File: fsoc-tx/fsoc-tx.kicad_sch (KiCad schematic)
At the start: 0 parts

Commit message: TX ROOT: MCU clock and POWER USB
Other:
- added sheet TX_LASER (tx_laser.kicad_sch)
- added sheet TX_MCU_CLOCK (tx_mcu_clock.kicad_sch)
- added sheet TX_POWER_USB (tx_power_usb.kicad_sch)
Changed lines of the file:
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@@
 	(generator_version "10.0")
 	(paper "A4")
+	(sheet
+		(at 118.11 31.75)
+		(size 40.64 49.53)
+		(exclude_from_sim no)
+		(in_bom yes)
+		(on_board yes)
+		(dnp no)
+		(fields_autoplaced yes)
+		(stroke
+			(width 0.1524)
+			(type solid)
+		)
+		(fill
+			(color 0 0 0 0)
+		)
+		(property "Sheetname" "TX_MCU_CLOCK"
+			(at 118.11 31.0384 0)
+			(show_name no)
+			(do_not_autoplace no)
+			(effects
+				(font
+					(size 1.27 1.27)
+				)
+				(justify left bottom)
+			)
+		)
+		(property "Sheetfile" "tx_mcu_clock.kicad_sch"
+			(at 118.11 81.8646 0)
+			(show_name no)
+			(do_not_autoplace no)
+			(effects
+				(font
+					(size 1.27 1.27)
+				)
+				(justify left top)
+			)
+		)
+		(instances
+			(project "fsoc-tx"
+				(path "/d92cb11a-a3ee-43a3-bd30-881774176ced"
+					(page "3")
+				)
+			)
+		)
+	)
+	(sheet
+		(at 58.42 30.48)
+		(size 39.37 52.07)
+		(exclude_from_sim no)
+		(in_bom yes)
+		(on_board yes)
+		(dnp no)
+		(fields_autoplaced yes)
+		(stroke
+			(width 0.1524)
+			(type solid)
+		)
+		(fill
+			(color 0 0 0 0)
+		)
+		(property "Sheetname" "TX_POWER_USB"
+			(at 58.42 29.7684 0)
+			(show_name no)
+			(do_not_autoplace no)
+			(effects
+				(font
+					(size 1.27 1.27)
+				)
+				(justify left bottom)
+			)
+		)
+		(property "Sheetfile" "tx_power_usb.kicad_sch"
+			(at 58.42 83.1346 0)
+			(show_name no)
+			(do_not_autoplace no)
+			(effects
+				(font
+					(size 1.27 1.27)
+				)
+				(justify left top)
+			)
+		)
+		(instances
+			(project "fsoc-tx"
+				(path "/d92cb11a-a3ee-43a3-bd30-881774176ced"
+					(page "2")
+				)
+			)
+		)
+	)
+	(sheet
+		(at 187.96 36.83)
+		(size 36.83 50.8)
+		(exclude_from_sim no)
+		(in_bom yes)
+		(on_board yes)
+		(dnp no)
+		(fields_autoplaced yes)
+		(stroke
+			(width 0.1524)
+			(type solid)
+		)
+		(fill
+			(color 0 0 0 0)
+		)
+		(property "Sheetname" "TX_LASER"
+			(at 187.96 36.1184 0)
+			(show_name no)
+			(do_not_autoplace no)
+			(effects
+				(font
+					(size 1.27 1.27)
+				)
+				(justify left bottom)
+			)
+		)
+		(property "Sheetfile" "tx_laser.kicad_sch"
+			(at 187.96 88.2146 0)
+			(show_name no)
+			(do_not_autoplace no)
+			(effects
+				(font
+					(size 1.27 1.27)
+				)
+				(justify left top)
+			)
+		)
+		(instances
+			(project "fsoc-tx"
+				(path "/d92cb11a-a3ee-43a3-bd30-881774176ced"
+					(page "4")
+				)
+			)
+		)
+	)
 	(sheet_instances
 		(path "/"

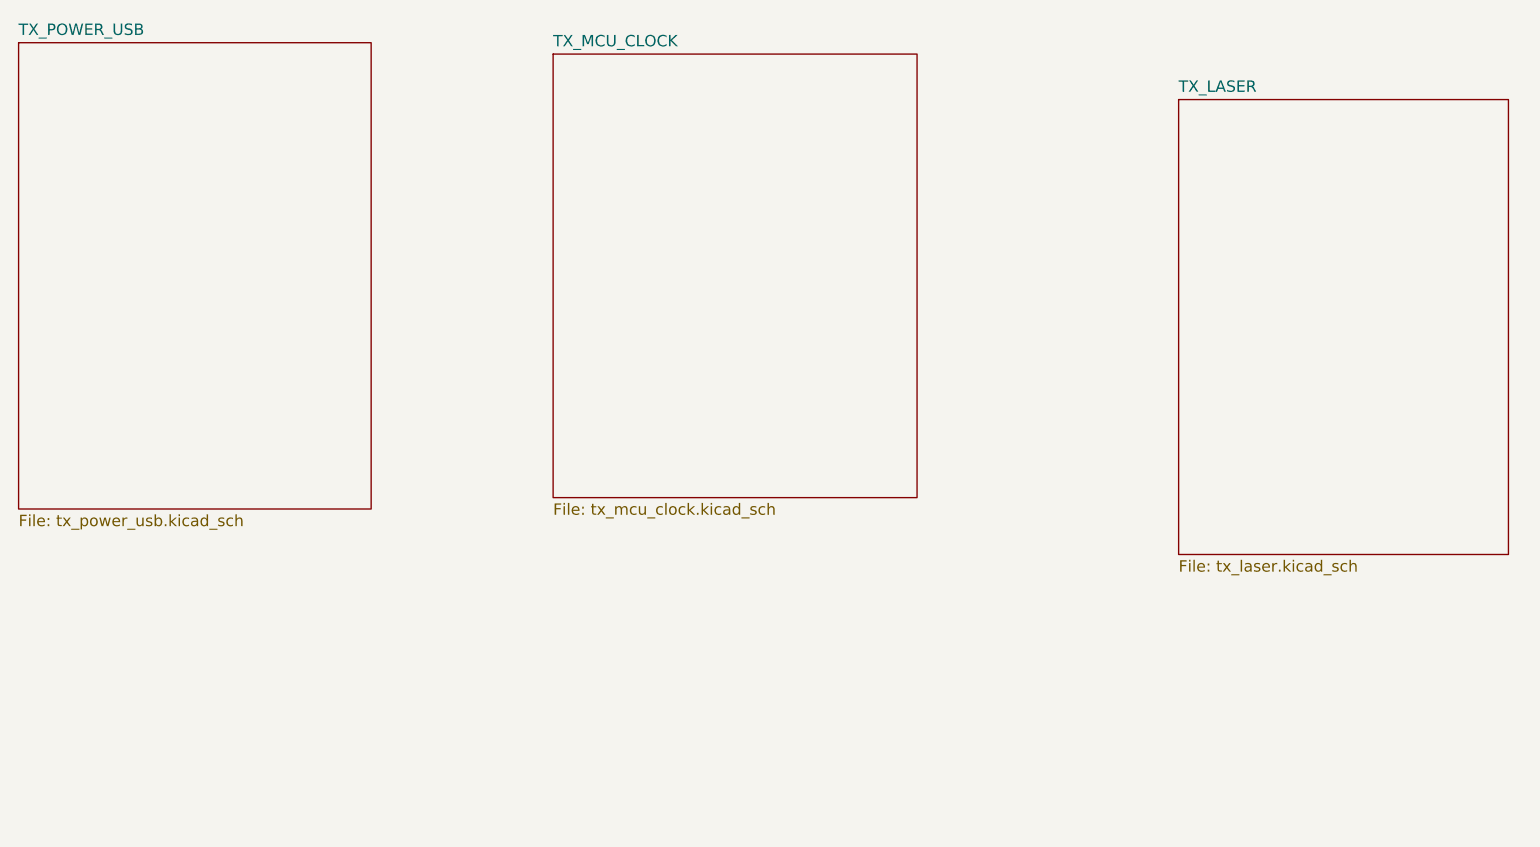
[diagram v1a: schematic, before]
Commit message: TX ROOT: laser + host IO
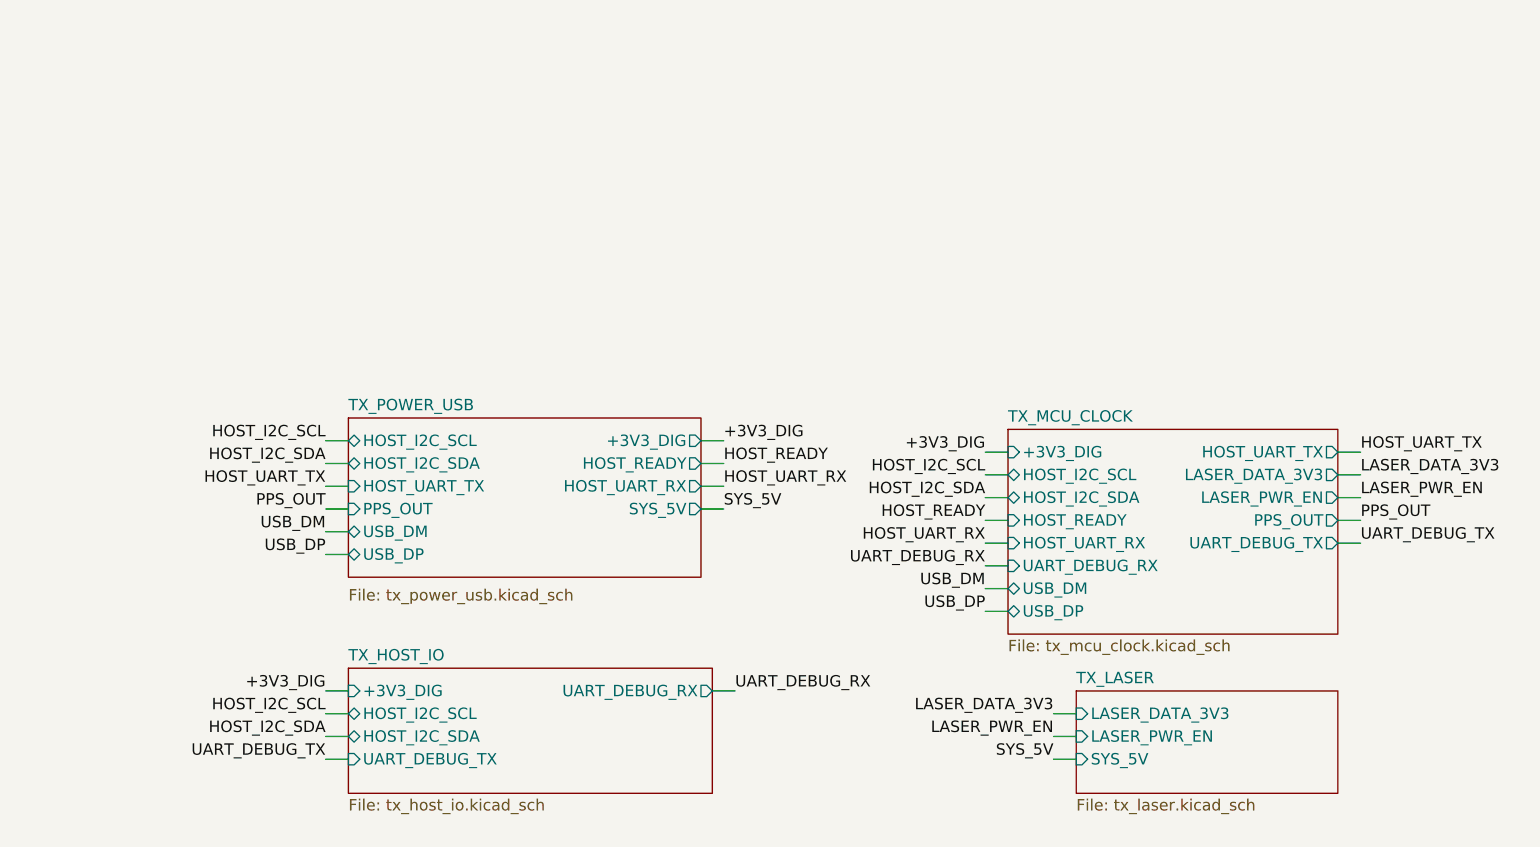
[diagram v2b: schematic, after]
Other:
- added sheet TX_HOST_IO (tx_host_io.kicad_sch)
- sheet TX_LASER ports: added LASER_DATA_3V3, LASER_PWR_EN, SYS_5V; removed none
- sheet TX_MCU_CLOCK ports: added +3V3_DIG, HOST_I2C_SCL, HOST_I2C_SDA, HOST_READY, HOST_UART_RX, HOST_UART_TX, LASER_DATA_3V3, LASER_PWR_EN, PPS_OUT, UART_DEBUG_RX, UART_DEBUG_TX, USB_DM, USB_DP; removed none
- sheet TX_POWER_USB ports: added +3V3_DIG, HOST_I2C_SCL, HOST_I2C_SDA, HOST_READY, HOST_UART_RX, HOST_UART_TX, PPS_OUT, SYS_5V, USB_DM, USB_DP; removed none

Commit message: TX PCB: DONE
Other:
- sheet TX_MCU_CLOCK ports: added USB_DN; removed USB_DM
- sheet TX_POWER_USB ports: added USB_DN; removed USB_DM
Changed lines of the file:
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@@
 		)
 	)
-	(label "USB_DM"
+	(label "USB_DN"
 		(at 92.71 85.09 180)
 		(effects
@@
 		)
 	)
-	(label "USB_DM"
+	(label "USB_DN"
 		(at 166.37 91.44 180)
 		(effects
@@
 	(sheet
 		(at 168.91 73.66)
-		(size 36.83 22.86)
+		(size 36.83 21.59)
 		(exclude_from_sim no)
 		(in_bom yes)
@@
 		)
 		(property "Sheetfile" "tx_mcu_clock.kicad_sch"
-			(at 168.91 97.1046 0)
+			(at 168.91 95.8346 0)
 			(show_name no)
 			(do_not_autoplace no)
@@
 			)
 		)
-		(pin "USB_DM" bidirectional
-			(at 168.91 91.44 180)
-			(effects
-				(font
-					(size 1.27 1.27)
-				)
-				(justify left)
-			)
-		)
 		(pin "USB_DP" bidirectional
 			(at 168.91 93.98 180)
@@
 				)
 				(justify right)
+			)
+		)
+		(pin "USB_DN" bidirectional
+			(at 168.91 91.44 180)
+			(effects
+				(font
+					(size 1.27 1.27)
+				)
+				(justify left)
 			)
 		)
@@
 		)
 		(property "Sheetfile" "tx_power_usb.kicad_sch"
-			(at 95.25 91.44 0)
+			(at 95.25 91.186 0)
 			(show_name no)
 			(do_not_autoplace no)
@@
 			)
 		)
-		(pin "USB_DM" bidirectional
-			(at 95.25 85.09 180)
-			(effects
-				(font
-					(size 1.27 1.27)
-				)
-				(justify left)
-			)
-		)
 		(pin "USB_DP" bidirectional
 			(at 95.25 87.63 180)
@@
 			)
 		)
+		(pin "USB_DN" bidirectional
+			(at 95.25 85.09 180)
+			(effects
+				(font
+					(size 1.27 1.27)
+				)
+				(justify left)
+			)
+		)

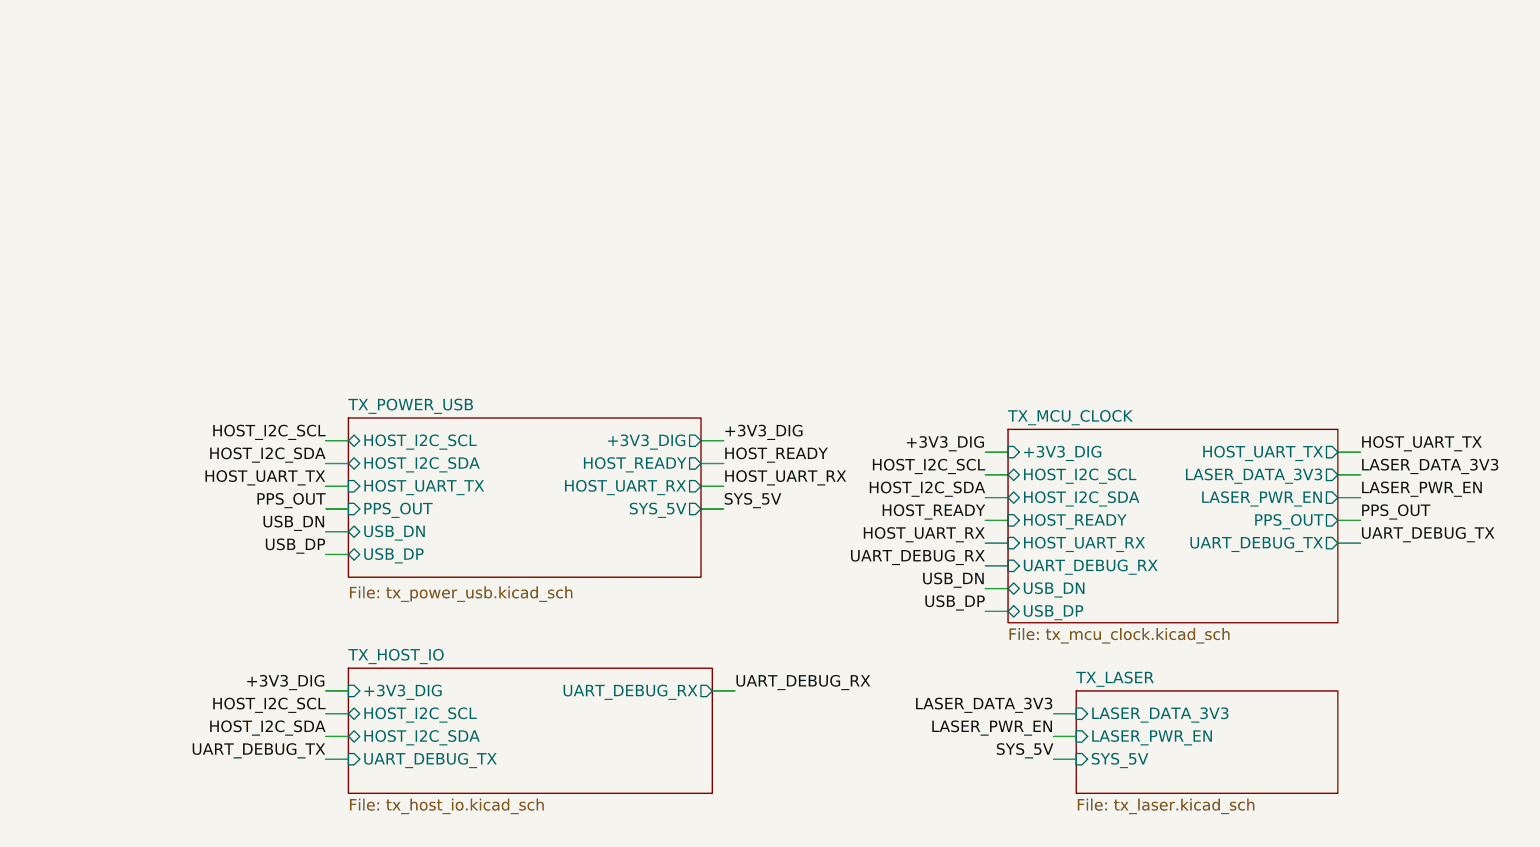
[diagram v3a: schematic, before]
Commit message: Switching ASTX-H11 to SiT5346 and SiT5346 datasheet
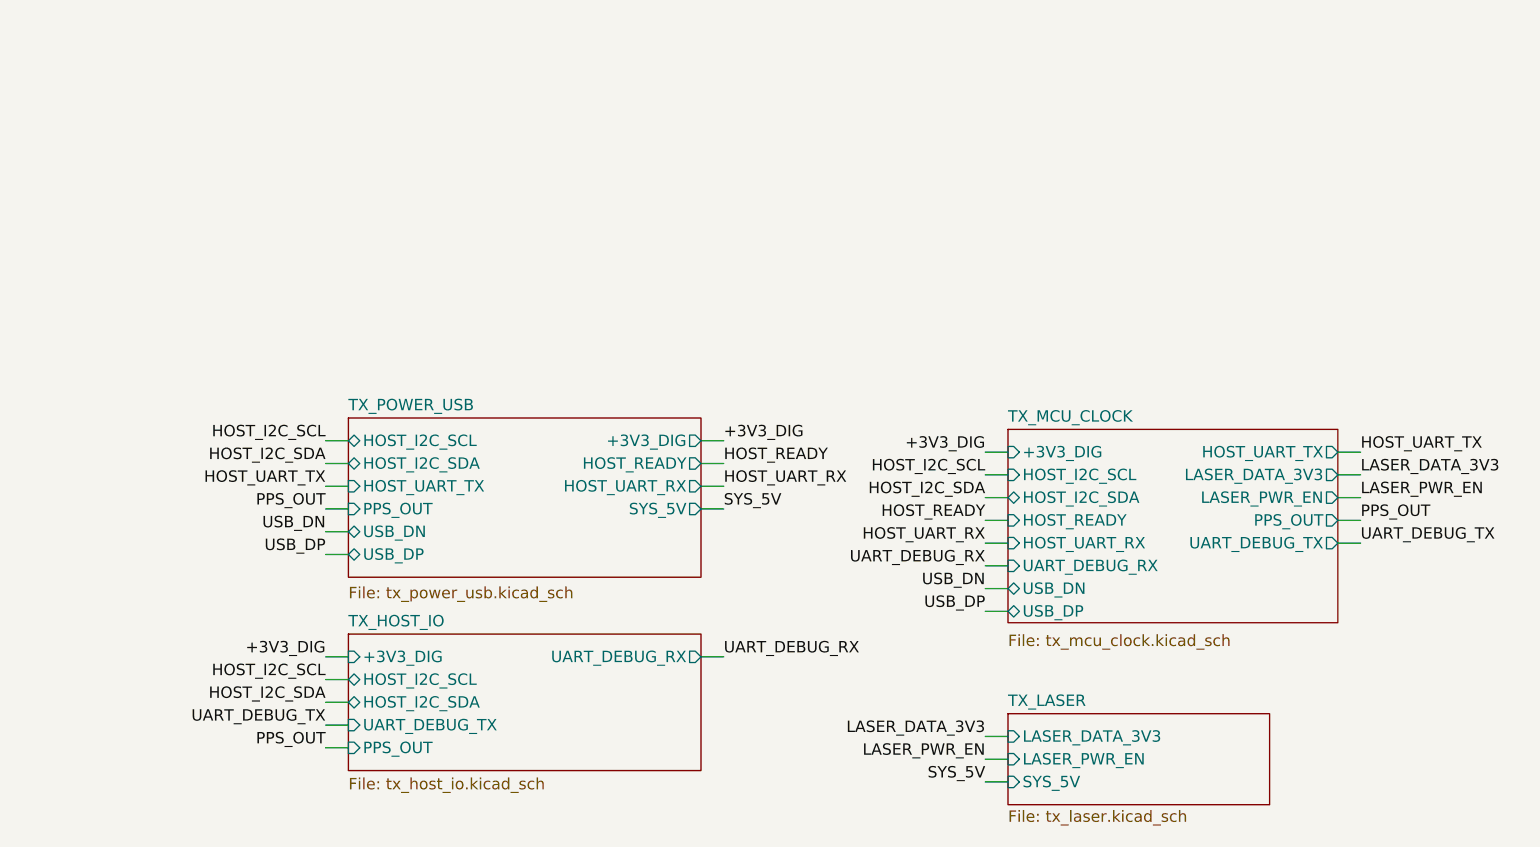
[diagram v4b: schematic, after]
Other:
- sheet TX_HOST_IO ports: added PPS_OUT; removed none
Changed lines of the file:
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@@
 	(wire
 		(pts
-			(xy 92.71 110.49) (xy 95.25 110.49)
+			(xy 92.71 106.68) (xy 95.25 106.68)
 		)
 		(stroke
@@
 	(wire
 		(pts
-			(xy 173.99 105.41) (xy 176.53 105.41)
+			(xy 166.37 107.95) (xy 168.91 107.95)
 		)
 		(stroke
@@
 	(wire
 		(pts
-			(xy 173.99 110.49) (xy 176.53 110.49)
+			(xy 166.37 113.03) (xy 168.91 113.03)
 		)
 		(stroke
@@
 	(wire
 		(pts
-			(xy 173.99 107.95) (xy 176.53 107.95)
+			(xy 166.37 110.49) (xy 168.91 110.49)
 		)
 		(stroke
@@
 	(wire
 		(pts
-			(xy 92.71 107.95) (xy 95.25 107.95)
+			(xy 92.71 104.14) (xy 95.25 104.14)
 		)
 		(stroke
@@
 	(wire
 		(pts
-			(xy 138.43 102.87) (xy 135.89 102.87)
+			(xy 137.16 99.06) (xy 134.62 99.06)
 		)
 		(stroke
@@
 	(wire
 		(pts
-			(xy 92.71 102.87) (xy 95.25 102.87)
-		)
-		(stroke
-			(width 0)
-			(type default)
-		)
-	)
-	(wire
-		(pts
-			(xy 92.71 105.41) (xy 95.25 105.41)
+			(xy 92.71 99.06) (xy 95.25 99.06)
+		)
+		(stroke
+			(width 0)
+			(type default)
+		)
+	)
+	(wire
+		(pts
+			(xy 92.71 101.6) (xy 95.25 101.6)
+		)
+		(stroke
+			(width 0)
+			(type default)
+		)
+	)
+	(wire
+		(pts
+			(xy 92.71 109.22) (xy 95.25 109.22)
 		)
 		(stroke
@@
 	)
 	(label "SYS_5V"
-		(at 173.99 110.49 180)
+		(at 166.37 113.03 180)
 		(effects
 			(font
@@
 	)
 	(label "UART_DEBUG_RX"
-		(at 138.43 102.87 0)
+		(at 137.16 99.06 0)
 		(effects
 			(font
@@
 	)
 	(label "HOST_I2C_SCL"
-		(at 92.71 105.41 180)
+		(at 92.71 101.6 180)
 		(effects
 			(font
@@
 		)
 	)
+	(label "PPS_OUT"
+		(at 92.71 109.22 180)
+		(effects
+			(font
+				(size 1.27 1.27)
+			)
+			(justify right bottom)
+		)
+	)
 	(label "HOST_UART_TX"
 		(at 208.28 76.2 0)
@@
 	)
 	(label "+3V3_DIG"
-		(at 92.71 102.87 180)
+		(at 92.71 99.06 180)
 		(effects
 			(font
@@
 	)
 	(label "UART_DEBUG_TX"
-		(at 92.71 110.49 180)
+		(at 92.71 106.68 180)
 		(effects
 			(font
@@
 	)
 	(label "LASER_PWR_EN"
-		(at 173.99 107.95 180)
+		(at 166.37 110.49 180)
 		(effects
 			(font
@@
 	)
 	(label "HOST_I2C_SDA"
-		(at 92.71 107.95 180)
+		(at 92.71 104.14 180)
 		(effects
 			(font
@@
 	)
 	(label "LASER_DATA_3V3"
-		(at 173.99 105.41 180)
+		(at 166.37 107.95 180)
 		(effects
 			(font
@@
 		(on_board yes)
 		(dnp no)
-		(fields_autoplaced yes)
 		(stroke
 			(width 0.1524)
@@
 		)
 		(property "Sheetfile" "tx_mcu_clock.kicad_sch"
-			(at 168.91 95.8346 0)
+			(at 168.91 96.52 0)
 			(show_name no)
 			(do_not_autoplace no)
@@
 			)
 		)
-		(pin "HOST_I2C_SCL" bidirectional
+		(pin "HOST_I2C_SCL" input
 			(at 168.91 78.74 180)
 			(effects
@@
 	)
 	(sheet
-		(at 95.25 100.33)
-		(size 40.64 13.97)
+		(at 95.25 96.52)
+		(size 39.37 15.24)
+		(exclude_from_sim no)
+		(in_bom yes)
+		(on_board yes)
+		(dnp no)
+		(stroke
+			(width 0.1524)
+			(type solid)
+		)
+		(fill
+			(color 0 0 0 0)
+		)
+		(property "Sheetname" "TX_HOST_IO"
+			(at 95.25 95.8084 0)
+			(show_name no)
+			(do_not_autoplace no)
+			(effects
+				(font
+					(size 1.27 1.27)
+				)
+				(justify left bottom)
+			)
+		)
+		(property "Sheetfile" "tx_host_io.kicad_sch"
+			(at 95.25 112.522 0)
+			(show_name no)
+			(do_not_autoplace no)
+			(effects
+				(font
+					(size 1.27 1.27)
+				)
+				(justify left top)
+			)
+		)
+		(pin "+3V3_DIG" input
+			(at 95.25 99.06 180)
+			(effects
+				(font
+					(size 1.27 1.27)
+				)
+				(justify left)
+			)
+		)
+		(pin "HOST_I2C_SCL" bidirectional
+			(at 95.25 101.6 180)
+			(effects
+				(font
+					(size 1.27 1.27)
+				)
+				(justify left)
+			)
+		)
+		(pin "HOST_I2C_SDA" bidirectional
+			(at 95.25 104.14 180)
+			(effects
+				(font
+					(size 1.27 1.27)
+				)
+				(justify left)
+			)
+		)
+		(pin "UART_DEBUG_TX" input
+			(at 95.25 106.68 180)
+			(effects
+				(font
+					(size 1.27 1.27)
+				)
+				(justify left)
+			)
+		)
+		(pin "UART_DEBUG_RX" output
+			(at 134.62 99.06 0)
+			(effects
+				(font
+					(size 1.27 1.27)
+				)
+				(justify right)
+			)
+		)
+		(pin "PPS_OUT" input
+			(at 95.25 109.22 180)
+			(effects
+				(font
+					(size 1.27 1.27)
+				)
+				(justify left)
+			)
+		)
+		(instances
+			(project "fsoc-tx"
+				(path "/d92cb11a-a3ee-43a3-bd30-881774176ced"
+					(page "5")
+				)
+			)
+		)
+	)
+	(sheet
+		(at 168.91 105.41)
+		(size 29.21 10.16)
 		(exclude_from_sim no)
 		(in_bom yes)
@@
 			(color 0 0 0 0)
 		)
-		(property "Sheetname" "TX_HOST_IO"
-			(at 95.25 99.6184 0)
+		(property "Sheetname" "TX_LASER"
+			(at 168.91 104.6984 0)
 			(show_name no)
 			(do_not_autoplace no)
@@
 			)
 		)
-		(property "Sheetfile" "tx_host_io.kicad_sch"
-			(at 95.25 114.8846 0)
+		(property "Sheetfile" "tx_laser.kicad_sch"
+			(at 168.91 116.1546 0)
 			(show_name no)
 			(do_not_autoplace no)
@@
 			)
 		)
-		(pin "+3V3_DIG" input
-			(at 95.25 102.87 180)
-			(effects
-				(font
-					(size 1.27 1.27)
-				)
-				(justify left)
-			)
-		)
-		(pin "HOST_I2C_SCL" bidirectional
-			(at 95.25 105.41 180)
-			(effects
-				(font
-					(size 1.27 1.27)
-				)
-				(justify left)
-			)
-		)
-		(pin "HOST_I2C_SDA" bidirectional
-			(at 95.25 107.95 180)
-			(effects
-				(font
-					(size 1.27 1.27)
-				)
-				(justify left)
-			)
-		)
-		(pin "UART_DEBUG_TX" input
-			(at 95.25 110.49 180)
-			(effects
-				(font
-					(size 1.27 1.27)
-				)
-				(justify left)
-			)
-		)
-		(pin "UART_DEBUG_RX" output
-			(at 135.89 102.87 0)
-			(effects
-				(font
-					(size 1.27 1.27)
-				)
-				(justify right)
-			)
-		)
-		(instances
-			(project "fsoc-tx"
-				(path "/d92cb11a-a3ee-43a3-bd30-881774176ced"
-					(page "5")
-				)
-			)
-		)
-	)
-	(sheet
-		(at 176.53 102.87)
-		(size 29.21 11.43)
-		(exclude_from_sim no)
-		(in_bom yes)
-		(on_board yes)
-		(dnp no)
-		(fields_autoplaced yes)
-		(stroke
-			(width 0.1524)
-			(type solid)
-		)
-		(fill
-			(color 0 0 0 0)
-		)
-		(property "Sheetname" "TX_LASER"
-			(at 176.53 102.1584 0)
-			(show_name no)
-			(do_not_autoplace no)
-			(effects
-				(font
-					(size 1.27 1.27)
-				)
-				(justify left bottom)
-			)
-		)
-		(property "Sheetfile" "tx_laser.kicad_sch"
-			(at 176.53 114.8846 0)
-			(show_name no)
-			(do_not_autoplace no)
-			(effects
-				(font
-					(size 1.27 1.27)
-				)
-				(justify left top)
-			)
-		)
 		(pin "LASER_DATA_3V3" input
-			(at 176.53 105.41 180)
+			(at 168.91 107.95 180)
 			(effects
 				(font
@@
 		)
 		(pin "LASER_PWR_EN" input
-			(at 176.53 107.95 180)
+			(at 168.91 110.49 180)
 			(effects
 				(font
@@
 		)
 		(pin "SYS_5V" input
-			(at 176.53 110.49 180)
-			(effects
-				(font
+			(at 168.91 113.03 180)
+			(effects
+				(font
